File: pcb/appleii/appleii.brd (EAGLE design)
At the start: 75 x 47 mm, 19 parts, among them J1 POWER_JACKPTH, J2 ATX24RH

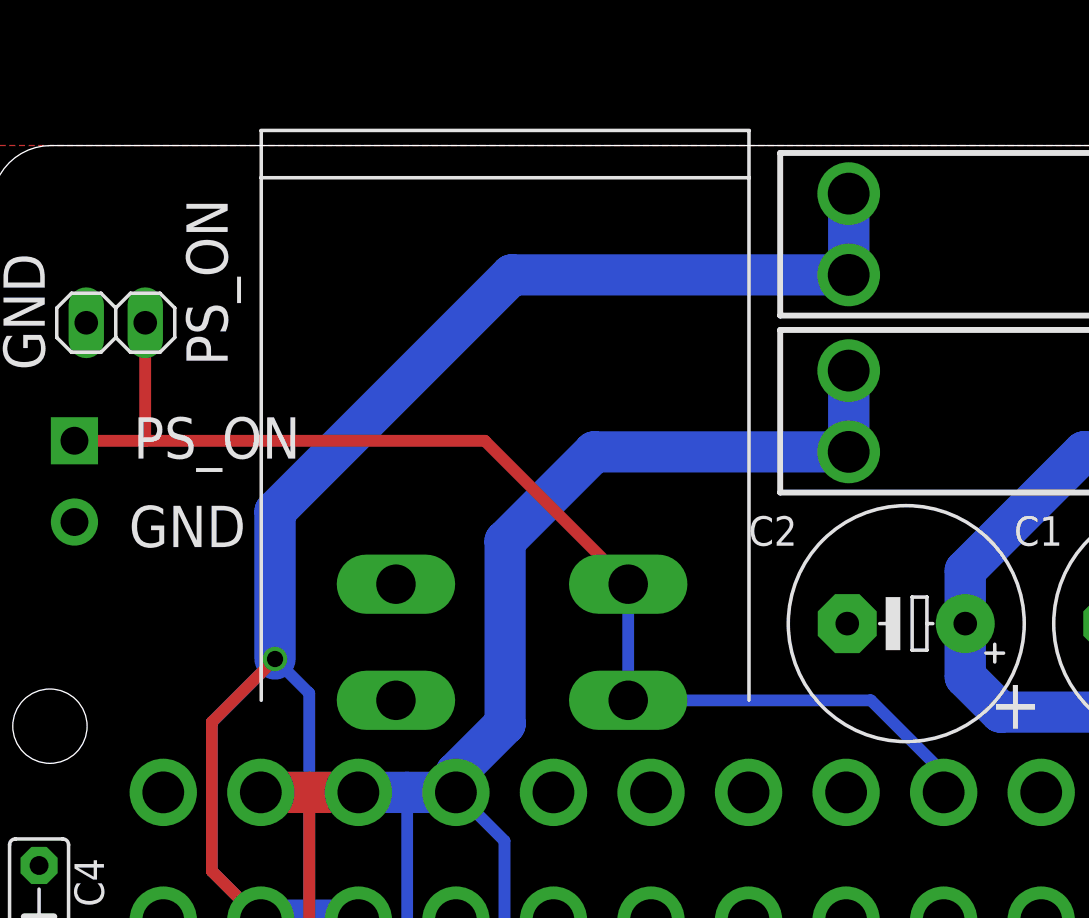
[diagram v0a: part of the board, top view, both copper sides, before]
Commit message: updated switch location
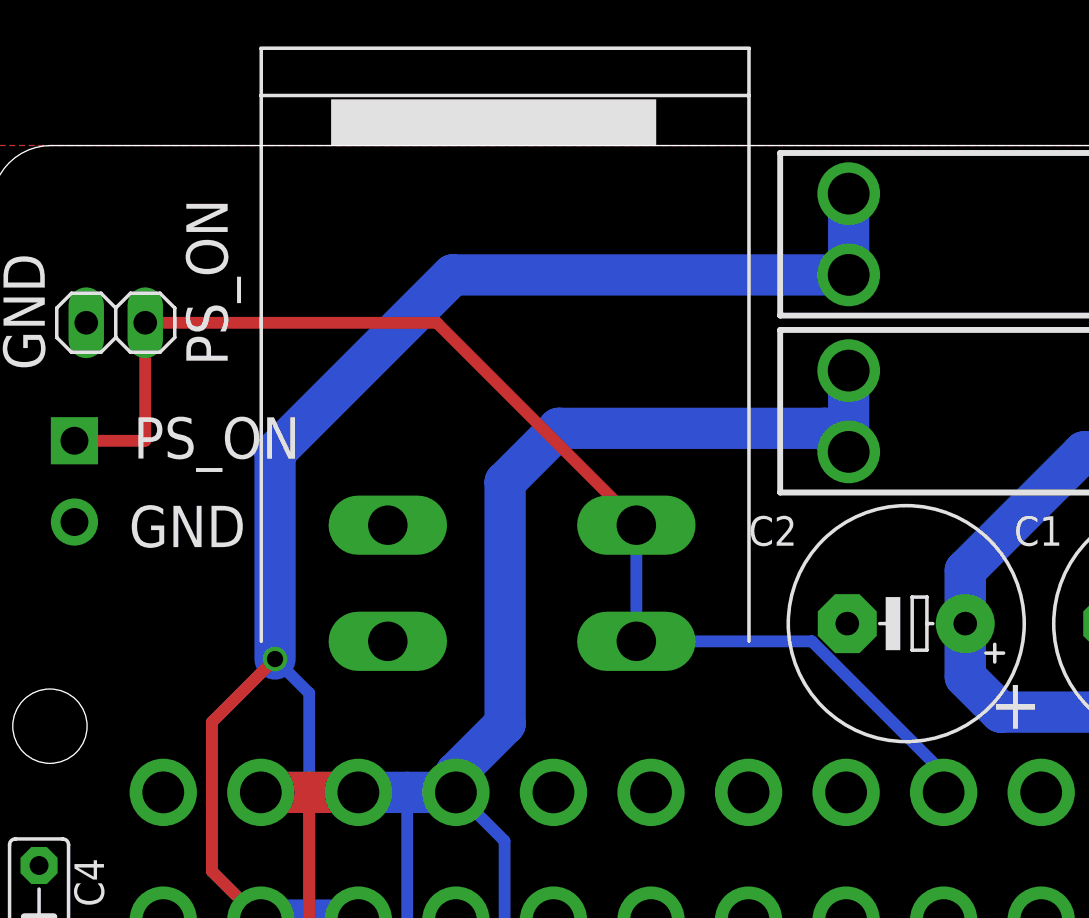
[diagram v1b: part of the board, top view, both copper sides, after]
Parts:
- moved U$5 2.54 mm to (22.1, 25.7)
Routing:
- net N$6: track 96.1 -> 98.4 mm
- net N$5: track 52.2 -> 54.4 mm
- net N$8: track 102.3 -> 103.8 mm
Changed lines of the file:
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@@
 <setting verticaltext="up"/>
 </settings>
-<grid distance="10" unitdist="mil" unit="mil" style="lines" multiple="1" display="no" altdistance="1" altunitdist="mil" altunit="mil"/>
+<grid distance="20" unitdist="mil" unit="mil" style="lines" multiple="1" display="no" altdistance="1" altunitdist="mil" altunit="mil"/>
 <layers>
 <layer number="1" name="Top" color="4" fill="1" visible="yes" active="yes"/>
@@
 <text x="9.263" y="41.113" size="1.778" layer="25" rot="R270" align="center">PS_ON</text>
 <text x="9.687" y="34.409" size="1.778" layer="25" align="center">PS_ON</text>
-<text x="60.706" y="44.196" size="1.4224" layer="26" distance="35" rot="MR0" align="center">12V
-Center
+<text x="60.198" y="44.704" size="1.4224" layer="26" distance="35" rot="MR0" align="center">12V Center
 Positive</text>
 <text x="68.485" y="44.4842" size="1.27" layer="26" distance="35" rot="MR0" align="center">GND</text>
@@
 <text x="59.341" y="29.4982" size="1.778" layer="25" distance="35" align="center">-12</text>
 <text x="63.913" y="29.4982" size="1.778" layer="25" distance="35" align="center">-5</text>
+<rectangle x1="14.605" y1="46.99" x2="28.605" y2="48.99" layer="25"/>
 </plain>
 <attributes>
@@
 <element name="U$3" library="a" package="M3_MOUNTING_HOLE_PACK" value="M3_MOUNTING_HOLE" x="72.5" y="22" smashed="yes"/>
 <element name="U$4" library="atx4vc" package="APPLEII" value="APPLEII" x="61.976" y="21.336" smashed="yes" rot="R270"/>
-<element name="U$5" library="atx4vc" package="ROCK_SWITCH" value="ROCK_SW" x="22.098" y="23.114" smashed="yes"/>
+<element name="U$5" library="atx4vc" package="ROCK_SWITCH" value="ROCK_SW" x="22.098" y="25.654" smashed="yes"/>
 <element name="IC1" library="v-reg" library_urn="urn:adsk.eagle:library:409" package="79XXS" package3d_urn="urn:adsk.eagle:package:30343/1" value="" x="74.422" y="31.4198" smashed="yes" rot="R270">
 <attribute name="POPULARITY" value="3" x="74.422" y="31.4198" size="1.778" layer="27" rot="R270" display="off"/>
@@
 <wire x1="19.98" y1="19.15" x2="19.98" y2="19.98" width="1.778" layer="16"/>
 <wire x1="19.98" y1="19.98" x2="22.098" y2="22.098" width="1.778" layer="16"/>
-<wire x1="22.098" y1="22.098" x2="22.098" y2="29.972" width="1.778" layer="16"/>
-<wire x1="25.936" y1="33.81" x2="36.892" y2="33.81" width="1.778" layer="16"/>
-<wire x1="22.098" y1="29.972" x2="25.936" y2="33.81" width="1.778" layer="16"/>
+<wire x1="22.098" y1="22.098" x2="22.098" y2="32.512" width="1.778" layer="16"/>
+<wire x1="35.876" y1="34.826" x2="36.892" y2="33.81" width="1.778" layer="16"/>
+<wire x1="35.876" y1="34.826" x2="24.412" y2="34.826" width="1.778" layer="16"/>
+<wire x1="22.098" y1="32.512" x2="24.412" y2="34.826" width="1.778" layer="16"/>
 <wire x1="11.58" y1="19.15" x2="13.6652" y2="19.15" width="1.778" layer="1"/>
 <wire x1="13.6652" y1="19.15" x2="15.78" y2="19.15" width="1.778" layer="1"/>
@@
 <wire x1="11.58" y1="13.65" x2="9.4742" y2="15.7558" width="0.508" layer="16"/>
 <wire x1="13.716" y1="13.65" x2="13.6652" y2="13.7008" width="0.508" layer="16"/>
-<wire x1="22.38" y1="41.43" x2="12.192" y2="31.242" width="1.778" layer="16"/>
-<wire x1="12.192" y1="24.892" x2="12.192" y2="31.242" width="1.778" layer="16"/>
-<wire x1="36.892" y1="41.43" x2="22.38" y2="41.43" width="1.778" layer="16"/>
+<wire x1="19.84" y1="41.43" x2="12.192" y2="33.782" width="1.778" layer="16"/>
+<wire x1="12.192" y1="24.892" x2="12.192" y2="33.782" width="1.778" layer="16"/>
+<wire x1="36.892" y1="41.43" x2="19.84" y2="41.43" width="1.778" layer="16"/>
 <wire x1="9.4742" y1="22.1742" x2="12.192" y2="24.892" width="0.508" layer="16"/>
 <wire x1="9.4742" y1="15.7558" x2="9.4742" y2="22.1742" width="0.508" layer="16"/>
@@
 <contactref element="U$5" pad="P$4"/>
 <wire x1="40.98" y1="19.15" x2="40.98" y2="19.98" width="0.508" layer="16"/>
-<wire x1="37.846" y1="23.114" x2="27.398" y2="23.114" width="0.508" layer="16"/>
-<wire x1="40.98" y1="19.98" x2="37.846" y2="23.114" width="0.508" layer="16"/>
-<wire x1="27.398" y1="23.114" x2="27.398" y2="28.114" width="0.508" layer="16"/>
-<wire x1="21.222" y1="34.29" x2="6.604" y2="34.29" width="0.508" layer="1"/>
+<wire x1="35.306" y1="25.654" x2="27.748" y2="25.654" width="0.508" layer="16"/>
+<wire x1="40.98" y1="19.98" x2="35.306" y2="25.654" width="0.508" layer="16"/>
+<wire x1="27.748" y1="25.654" x2="27.748" y2="30.654" width="0.508" layer="16"/>
 <wire x1="6.604" y1="34.29" x2="3.556" y2="34.29" width="0.508" layer="1"/>
-<wire x1="27.398" y1="28.114" x2="21.222" y2="34.29" width="0.508" layer="1"/>
 <wire x1="6.604" y1="39.37" x2="6.604" y2="34.29" width="0.508" layer="1"/>
+<wire x1="6.604" y1="39.37" x2="19.159" y2="39.37" width="0.508" layer="1"/>
+<wire x1="19.159" y1="39.37" x2="27.748" y2="30.781" width="0.508" layer="1"/>
+<wire x1="27.748" y1="30.781" x2="27.748" y2="30.654" width="0.508" layer="1"/>
 </signal>
 <signal name="-5V">

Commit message: updated pcb
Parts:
- removed C4, C5: (no value), capacitor-wima:C5B2.5
- removed J2: ATX24RH, macse:ATX24_RIGHT_ANGLE
- removed J3, J7: (no value), atx_power_control:SCREWTERMINAL-3.5MM-2-NS
- removed JP4: (no value), appleii:1X04
- removed U$8: CAR_FUSE_HOLDER3IN1, atx_power_control:FUSE_HOLDER_3IN1
- added JP3: (no value), appleii:1X04
- added U$6: APPLEII, atx4vc:APPLEII
- C1, C2: device rcl:E5-10,5 -> capacitor-wima:C5B2.5
- J1: value POWER_JACKPTH -> ATX24RH; device appleii:POWER_JACK_PTH -> macse:ATX24_RIGHT_ANGLE
- JP1: device appleii:1X04 -> pinhead:1X02
- JP2: device pinhead:1X02 -> pinhead:1X03
- U$1: value M3_MOUNTING_HOLE -> CAR_FUSE_HOLDER3IN1; device a:M3_MOUNTING_HOLE_PACK -> atx_power_control:FUSE_HOLDER_3IN1
- U$3: value M3_MOUNTING_HOLE -> ROCK_SW; device a:M3_MOUNTING_HOLE_PACK -> atx4vc:ROCK_SWITCH
- U$4: value APPLEII -> M3_MOUNTING_HOLE; device atx4vc:APPLEII -> a:M3_MOUNTING_HOLE_PACK
- U$5: value ROCK_SW -> M3_MOUNTING_HOLE; device atx4vc:ROCK_SWITCH -> a:M3_MOUNTING_HOLE_PACK
- moved JP2 67.3 mm to (65.8, 9.78), turned to 0 degrees
- moved JP1 66.6 mm to (3.05, 3.97), turned to 90 degrees
- moved C3 53.1 mm to (50.4, 26.2), turned to 0 degrees
- moved C1 51.0 mm to (2.03, 11.6), turned to 90 degrees
- moved U$3 50.4 mm to (22.1, 23.7)
- moved J1 49.1 mm to (31.1, 9.26), turned to 0 degrees
- moved U$1 43.0 mm to (43.9, 33.6), turned to 180 degrees
- moved IC1 35.1 mm to (39.4, 28.7), turned to 0 degrees
- moved C2 34.4 mm to (4.95, 27.8)
- moved U$5 20.4 mm to (2.50, 20.0)
- moved U$4 10.6 mm to (72.5, 20.0), turned to 0 degrees
- moved U$2 1.87 mm to (43.9, 41.3)
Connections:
- net +12V: now also JP2.3, U$6.4; no longer C1.+, JP1.2, U$4.4
- net +5V: now also JP2.1, U$1.A0, U$1.A1, U$6.3; no longer C2.+, JP4.2, U$4.3, U$8.A0, U$8.A1
- net -12V: now also J1.14, U$6.5; no longer J2.14, U$4.5
- net -5V: now also C3.1, U$6.6; no longer C5.1, U$4.6
- net GND: now also C1.2, C2.2, J1.15, J1.17, J1.18, J1.19, J1.24, J1.3, J1.5, J1.7, JP1.2, JP3.1, U$3.P$1, U$3.P$3, U$6.1, U$6.2; no longer C1.-, C2.-, C4.2, C5.2, J1.GND, J1.GNDBREAK, J2.15, J2.17, J2.18, J2.19, J2.24, J2.3, J2.5, J2.7, J3.2, J7.2, JP1.1, JP2.2, JP4.1, U$4.1, U$4.2, U$5.P$1, U$5.P$3
- net N$1: now also JP2.2, JP3.2; no longer J1.PWR, J3.1
- net N$5: now also J1.16, JP1.1, U$3.P$2, U$3.P$4; no longer J2.16, J7.1, JP2.1, U$5.P$2, U$5.P$4
- net N$6: now also C1.1, J1.21, J1.22, J1.23, J1.6, U$1.B0, U$1.B1; no longer C4.1, J2.21, J2.22, J2.23, J2.6, U$8.B0, U$8.B1
- net N$8: now also C2.1, J1.10, J1.11; no longer C3.1, J2.10, J2.11
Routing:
- net N$8: track 103.8 -> 84.8 mm
- net +5V: track 56.3 -> 38.0 mm
- net N$5: track 54.4 -> 72.2 mm
- net +12V: track 61.2 -> 52.4 mm
- net -5V: track 19.8 -> 27.4 mm
- net N$6: track 98.4 -> 93.2 mm
- net N$1: track 12.0 -> 7.39 mm
- net -12V: track 28.0 -> 30.8 mm
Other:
- board size 75 x 47 mm -> 75 x 45 mm
- board text added: "picoRC.com"
- board text removed: "12V"
- board text removed: "12V Center Positive"
- board text removed: "GND"
- board text removed: "RED"
